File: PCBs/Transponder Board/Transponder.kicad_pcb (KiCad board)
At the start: 2 copper layers, 64 x 87.4 mm, 27 parts, among them J1 Conn_01x02, J2 Conn_01x02, J3 Conn_01x02, J4 Conn_01x02, J5 Conn_01x02, J6 Conn_01x09, U1 R-78E3.3-0.5, U2 MicroSDBreakout, U3 XBee-S2C, U4 PI4ULS5V201TAEX

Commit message: transponder changes as per Alexs review
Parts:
- added J7: Conn_01x02, Connectors_JST:JST_PH_B2B-PH-K_02x2.00mm_Straight, F.Cu at (88.9, 62.7)
- J1: footprint molex:molex_kk_22-23-2021 -> Connectors_JST:JST_PH_B2B-PH-K_02x2.00mm_Straight
- U4: footprint sot:SOT-23-6 -> TO_SOT_Packages_SMD:SOT-23-6_Handsoldering
- moved REF** 38.7 mm to (119.0, 99.0)
- moved J3 34.6 mm to (115.6, 132.1)
- moved R5 19.7 mm to (118.1, 124.5), turned to 90 degrees
- moved J1 7.38 mm to (80.8, 62.7)
- moved REF** 3.26 mm to (62.0, 141.0)
- moved REF** 2.47 mm to (62.0, 61.0)
- turned C3 to 180 degrees
- turned C4 to 180 degrees
- turned C5 to 180 degrees
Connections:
- J1 pad 2: GND -> Net-(J1-Pad2)
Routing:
- net 7.4V: track 5.10 -> 83.1 mm, vias 0 -> 3
- net GND: track 93.4 -> 43.8 mm, vias 9 -> 13
- net D2: track 103.3 -> 130.8 mm, vias 2 -> 3
- net Net-(J1-Pad2): track 0.00 -> 6.13 mm
- net Net-(R1-Pad1): track 18.5 -> 20.9 mm
- net Net-(J1-Pad1): track 81.8 -> 80.6 mm
- net 3.3V: track 64.2 -> 65.3 mm
- net 5V: track 179.8 -> 178.6 mm
- net MOSI: track 50.4 -> 49.5 mm
- net MISO: track 53.1 -> 52.2 mm
- net LCD_D6: vias 0 -> 1
- removed copper zone on F.Cu, net 7.4V
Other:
- board size 64 x 87.4 mm -> 65 x 88 mm
- rule pad_to_mask_clearance: 0.2 -> 0.002
- board text added: "+ -"
- board text added: "How To Rotate Text in MS Kicad Adam Paul 2018"
- board text added: "Pin"
- board text removed: "First Time First Try Adam Paul 2018"
- board text removed: "GND 7V"
- board text removed: "LCD Pin"

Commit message: fixed outstanding changes on instr and transponder board
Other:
- rule pad_to_mask_clearance: 0.002 -> 0.0508
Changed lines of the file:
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@@
     (links 60)
     (no_connects 0)
-    (area 57.924999 56.924999 123.075001 145.075001)
+    (area 51.021143 55.825 128.557143 146.275)
     (thickness 1.6)
     (drawings 24)
@@
     (pad_size 1.524 1.524)
     (pad_drill 0.762)
-    (pad_to_mask_clearance 0.002)
+    (pad_to_mask_clearance 0.0508)
     (aux_axis_origin 0 0)
     (visible_elements 7FFFFF7F)

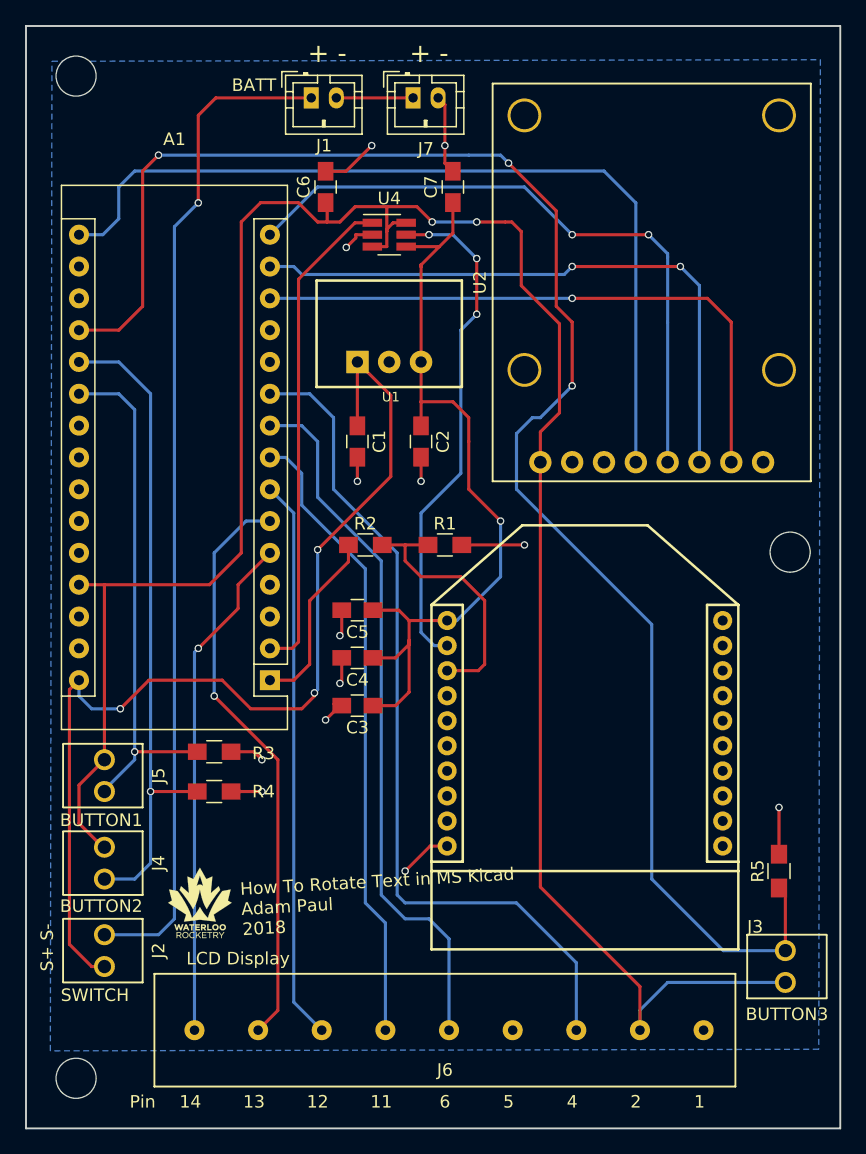
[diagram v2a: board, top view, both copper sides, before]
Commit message: swapped all mounting holes with plated ones, fixed disconnected components on recovery, added the 4 decoupling caps to recovery, fixed silk screen on pads in instr, fixed traces connecting through pads on recovery and instr, moved q1 on instr, brought trace in near u2 on instr, switched u2 & u3 to hand solder on instr, fixed xbee screen on recovery, fixed connector labels on recovery, removed recovery dims past edge cuts, fixed pad mask clearance on recovery
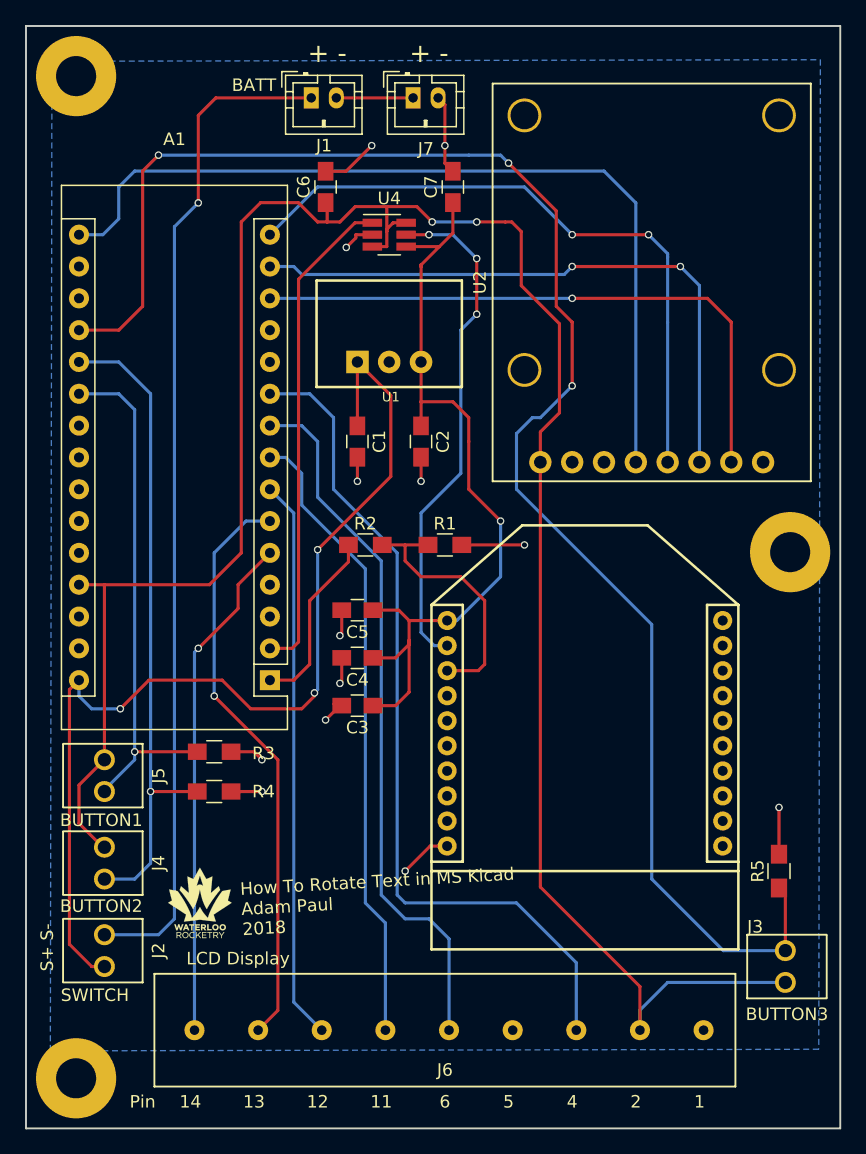
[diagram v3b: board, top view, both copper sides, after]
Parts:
- REF** (x3): footprint Mounting_Holes:MountingHole_3.2mm_M3 -> Mounting_Holes:MountingHole_3.2mm_M3_Pad
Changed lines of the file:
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@@
     (add_net XBEE-DOUT)
-  )
-  (module Mounting_Holes:MountingHole_3.2mm_M3 (layer F.Cu)
-    (at 62 61)
-    (descr "Mounting Hole 3.2mm, no annular, M3")
-    (tags "mounting hole 3.2mm no annular m3")
-    (attr virtual)
-    (fp_text reference REF** (at 0 -4.2) (layer F.SilkS) hide
-      (effects (font (size 1 1) (thickness 0.15)))
-    )
-    (fp_text value MountingHole_3.2mm_M3 (at 0 4.2) (layer F.Fab) hide
-      (effects (font (size 1 1) (thickness 0.15)))
-    )
-    (fp_text user %R (at 0.3 0) (layer F.Fab)
-      (effects (font (size 1 1) (thickness 0.15)))
-    )
-    (fp_circle (center 0 0) (end 3.2 0) (layer Cmts.User) (width 0.15))
-    (fp_circle (center 0 0) (end 3.45 0) (layer F.CrtYd) (width 0.05))
-    (pad 1 np_thru_hole circle (at 0 0) (size 3.2 3.2) (drill 3.2) (layers *.Cu *.Mask))
-  )
-  (module Mounting_Holes:MountingHole_3.2mm_M3 (layer F.Cu)
-    (at 119 99)
-    (descr "Mounting Hole 3.2mm, no annular, M3")
-    (tags "mounting hole 3.2mm no annular m3")
-    (attr virtual)
-    (fp_text reference REF** (at 0 -4.2) (layer F.SilkS) hide
-      (effects (font (size 1 1) (thickness 0.15)))
-    )
-    (fp_text value MountingHole_3.2mm_M3 (at 0 4.2) (layer F.Fab) hide
-      (effects (font (size 1 1) (thickness 0.15)))
-    )
-    (fp_text user %R (at 0.3 0) (layer F.Fab)
-      (effects (font (size 1 1) (thickness 0.15)))
-    )
-    (fp_circle (center 0 0) (end 3.2 0) (layer Cmts.User) (width 0.15))
-    (fp_circle (center 0 0) (end 3.45 0) (layer F.CrtYd) (width 0.05))
-    (pad 1 np_thru_hole circle (at 0 0) (size 3.2 3.2) (drill 3.2) (layers *.Cu *.Mask))
   )
   (module screwTerminals:VI0921550000G (layer F.Cu)
@@
     (pad 2 thru_hole circle (at 0 0) (size 1.8 1.8) (drill 0.9) (layers *.Cu *.Mask F.SilkS)
       (net 7 GND))
-  )
-  (module Mounting_Holes:MountingHole_3.2mm_M3 (layer F.Cu)
-    (at 62 141)
-    (descr "Mounting Hole 3.2mm, no annular, M3")
-    (tags "mounting hole 3.2mm no annular m3")
-    (attr virtual)
-    (fp_text reference REF** (at -8.636 -2.54) (layer F.SilkS) hide
-      (effects (font (size 1 1) (thickness 0.15)))
-    )
-    (fp_text value MountingHole_3.2mm_M3 (at 0 4.2) (layer F.Fab) hide
-      (effects (font (size 1 1) (thickness 0.15)))
-    )
-    (fp_text user %R (at 0.3 0) (layer F.Fab)
-      (effects (font (size 1 1) (thickness 0.15)))
-    )
-    (fp_circle (center 0 0) (end 3.2 0) (layer Cmts.User) (width 0.15))
-    (fp_circle (center 0 0) (end 3.45 0) (layer F.CrtYd) (width 0.05))
-    (pad 1 np_thru_hole circle (at 0 0) (size 3.2 3.2) (drill 3.2) (layers *.Cu *.Mask))
   )
   (module Logos:logo6 (layer F.Cu)
@@
       (net 50 "Net-(U3-Pad20)"))
   )
+  (module Mounting_Holes:MountingHole_3.2mm_M3_Pad (layer F.Cu)
+    (at 62 61)
+    (descr "Mounting Hole 3.2mm, M3")
+    (tags "mounting hole 3.2mm m3")
+    (attr virtual)
+    (fp_text reference REF** (at 0 -4.2) (layer F.SilkS) hide
+      (effects (font (size 1 1) (thickness 0.15)))
+    )
+    (fp_text value MountingHole_3.2mm_M3 (at 0 4.2) (layer F.Fab) hide
+      (effects (font (size 1 1) (thickness 0.15)))
+    )
+    (fp_text user %R (at 0.3 0) (layer F.Fab) hide
+      (effects (font (size 1 1) (thickness 0.15)))
+    )
+    (fp_circle (center 0 0) (end 3.2 0) (layer Cmts.User) (width 0.15))
+    (fp_circle (center 0 0) (end 3.45 0) (layer F.CrtYd) (width 0.05))
+    (pad 1 thru_hole circle (at 0 0) (size 6.4 6.4) (drill 3.2) (layers *.Cu *.Mask))
+  )
+  (module Mounting_Holes:MountingHole_3.2mm_M3_Pad (layer F.Cu)
+    (at 119 99)
+    (descr "Mounting Hole 3.2mm, M3")
+    (tags "mounting hole 3.2mm m3")
+    (attr virtual)
+    (fp_text reference REF** (at 0 -4.2) (layer F.SilkS) hide
+      (effects (font (size 1 1) (thickness 0.15)))
+    )
+    (fp_text value MountingHole_3.2mm_M3 (at 0 4.2) (layer F.Fab) hide
+      (effects (font (size 1 1) (thickness 0.15)))
+    )
+    (fp_text user %R (at 0.3 0) (layer F.Fab) hide
+      (effects (font (size 1 1) (thickness 0.15)))
+    )
+    (fp_circle (center 0 0) (end 3.2 0) (layer Cmts.User) (width 0.15))
+    (fp_circle (center 0 0) (end 3.45 0) (layer F.CrtYd) (width 0.05))
+    (pad 1 thru_hole circle (at 0 0) (size 6.4 6.4) (drill 3.2) (layers *.Cu *.Mask))
+  )
+  (module Mounting_Holes:MountingHole_3.2mm_M3_Pad (layer F.Cu)
+    (at 62 141)
+    (descr "Mounting Hole 3.2mm, M3")
+    (tags "mounting hole 3.2mm m3")
+    (attr virtual)
+    (fp_text reference REF** (at 0 -4.2) (layer F.SilkS) hide
+      (effects (font (size 1 1) (thickness 0.15)))
+    )
+    (fp_text value MountingHole_3.2mm_M3 (at 0 4.2) (layer F.Fab) hide
+      (effects (font (size 1 1) (thickness 0.15)))
+    )
+    (fp_text user %R (at 0.3 0) (layer F.Fab) hide
+      (effects (font (size 1 1) (thickness 0.15)))
+    )
+    (fp_circle (center 0 0) (end 3.2 0) (layer Cmts.User) (width 0.15))
+    (fp_circle (center 0 0) (end 3.45 0) (layer F.CrtYd) (width 0.05))
+    (pad 1 thru_hole circle (at 0 0) (size 6.4 6.4) (drill 3.2) (layers *.Cu *.Mask))
+  )
   (gr_text "+ -" (at 82.042 59.182) (layer F.SilkS)

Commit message: Added Gerber Files
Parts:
- moved G*** 3.22 mm to (72.4, 123.8)
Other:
- board text added: "Not Going to Space Today Adam Paul 2018"
- board text removed: "How To Rotate Text in MS Kicad Adam Paul 2018"
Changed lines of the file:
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@@
     (pcbplotparams
       (layerselection 0x00030_80000001)
-      (usegerberextensions false)
+      (usegerberextensions true)
       (excludeedgelayer true)
       (linewidth 0.100000)
@@
       (outputformat 1)
       (mirror false)
-      (drillshape 1)
+      (drillshape 0)
       (scaleselection 1)
-      (outputdirectory ""))
+      (outputdirectory "Gerber Files/"))
   )
   (net 0 "")
@@
   )
   (module Logos:logo6 (layer F.Cu)
-    (at 71.882 127)
+    (at 72.39 123.825)
     (fp_text reference G*** (at 5.588 4.572) (layer F.SilkS) hide
       (effects (font (thickness 0.3)))
@@
     (effects (font (size 1 1) (thickness 0.15)))
   )
-  (gr_text "How To Rotate Text in MS Kicad\nAdam Paul\n2018" (at 75.184 127.508 3.2) (layer F.SilkS)
+  (gr_text "Not Going \nto Space Today\nAdam Paul\n2018" (at 76.2 123.825) (layer F.SilkS)
     (effects (font (size 1 1) (thickness 0.1)) (justify left))
   )
